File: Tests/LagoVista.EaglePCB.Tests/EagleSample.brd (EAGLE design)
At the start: 100 x 80 mm, 4 parts

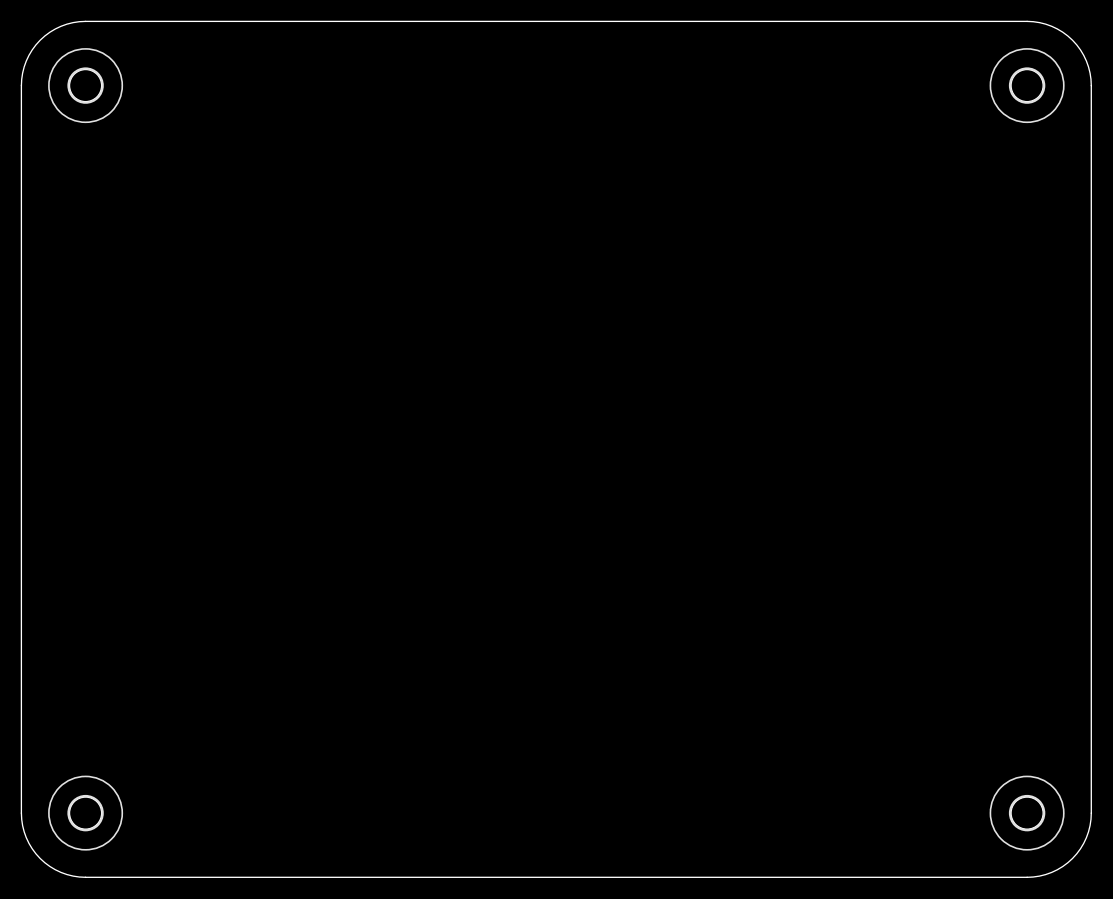
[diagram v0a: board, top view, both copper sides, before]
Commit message: rendering eagle lines
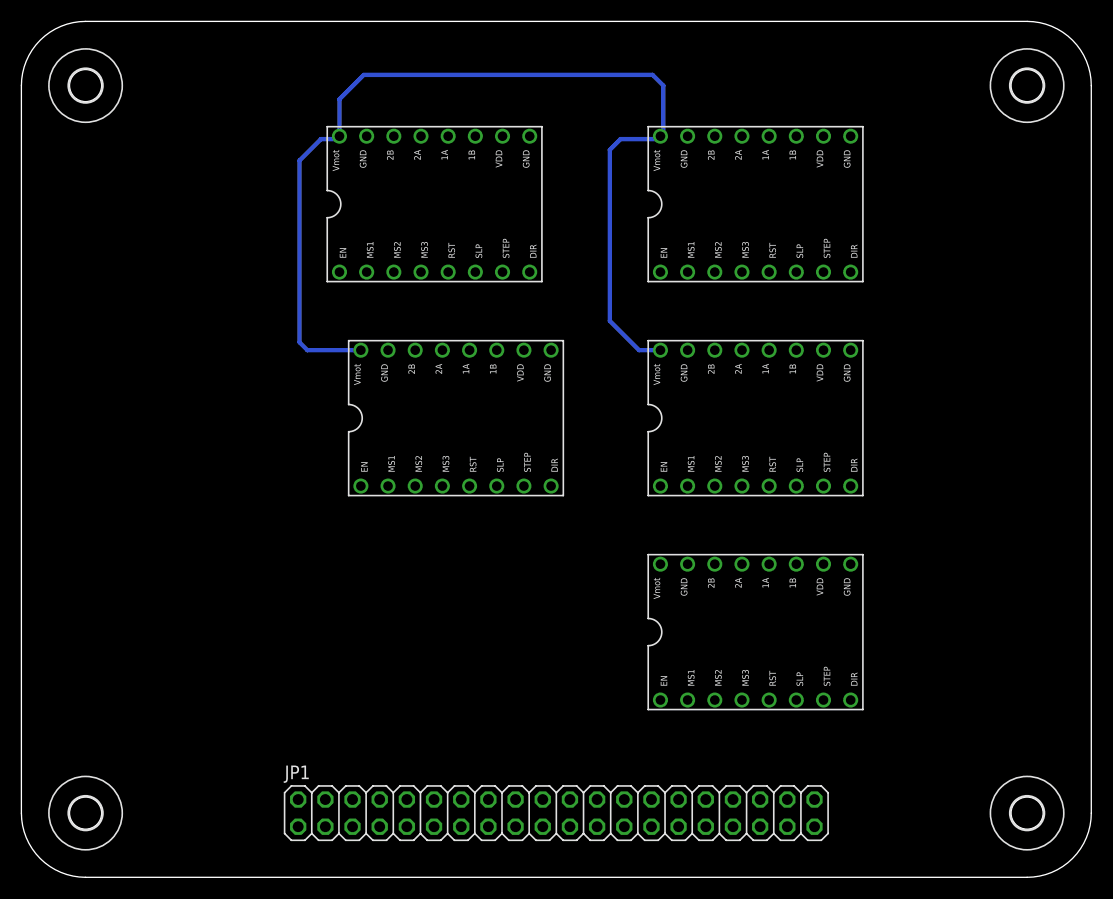
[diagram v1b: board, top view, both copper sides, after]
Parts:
- added JP1: (no value), pinhead:2X20
- added U$5, U$6, U$7, U$8, U$9: A4988BREAKOUT, RepRapjr:A4988BREAKOUT
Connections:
- new net GND: U$5.GND, U$5.GND@0, U$6.GND, U$6.GND@0, U$7.GND, U$7.GND@0, U$8.GND, U$8.GND@0, U$9.GND, U$9.GND@0
- new net VDD: U$5.VDD, U$6.VDD, U$7.VDD, U$8.VDD, U$9.VDD
- new net VMOT: U$5.VMOT, U$6.VMOT, U$7.VMOT, U$8.VMOT, U$9.VMOT
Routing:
- net VMOT: track 0.00 -> 94.7 mm
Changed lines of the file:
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@@
 <layer number="48" name="Document" color="7" fill="1" visible="yes" active="yes"/>
 <layer number="49" name="Reference" color="7" fill="1" visible="yes" active="yes"/>
+<layer number="50" name="dxf" color="7" fill="1" visible="yes" active="yes"/>
 <layer number="51" name="tDocu" color="7" fill="1" visible="yes" active="yes"/>
 <layer number="52" name="bDocu" color="7" fill="1" visible="yes" active="yes"/>
+<layer number="53" name="tGND_GNDA" color="7" fill="9" visible="no" active="no"/>
+<layer number="54" name="bGND_GNDA" color="1" fill="9" visible="no" active="no"/>
+<layer number="56" name="wert" color="7" fill="1" visible="yes" active="yes"/>
 <layer number="90" name="Modules" color="5" fill="1" visible="no" active="no"/>
 <layer number="91" name="Nets" color="2" fill="1" visible="no" active="no"/>
@@
 <layer number="97" name="Info" color="7" fill="1" visible="no" active="no"/>
 <layer number="98" name="Guide" color="6" fill="1" visible="no" active="no"/>
+<layer number="100" name="Muster" color="7" fill="1" visible="no" active="no"/>
+<layer number="101" name="Patch_Top" color="12" fill="4" visible="yes" active="yes"/>
+<layer number="102" name="Vscore" color="7" fill="1" visible="yes" active="yes"/>
+<layer number="103" name="tMap" color="7" fill="1" visible="yes" active="yes"/>
+<layer number="104" name="Name" color="7" fill="1" visible="yes" active="yes"/>
+<layer number="105" name="tPlate" color="7" fill="1" visible="yes" active="yes"/>
+<layer number="106" name="bPlate" color="7" fill="1" visible="yes" active="yes"/>
+<layer number="107" name="Crop" color="7" fill="1" visible="yes" active="yes"/>
+<layer number="116" name="Patch_BOT" color="9" fill="4" visible="yes" active="yes"/>
+<layer number="121" name="_tsilk" color="7" fill="1" visible="yes" active="yes"/>
+<layer number="122" name="_bsilk" color="7" fill="1" visible="yes" active="yes"/>
+<layer number="151" name="HeatSink" color="7" fill="1" visible="yes" active="yes"/>
+<layer number="200" name="200bmp" color="1" fill="10" visible="yes" active="yes"/>
+<layer number="201" name="201bmp" color="2" fill="10" visible="yes" active="yes"/>
+<layer number="202" name="202bmp" color="3" fill="10" visible="yes" active="yes"/>
+<layer number="203" name="203bmp" color="4" fill="10" visible="yes" active="yes"/>
+<layer number="204" name="204bmp" color="5" fill="10" visible="yes" active="yes"/>
+<layer number="205" name="205bmp" color="6" fill="10" visible="yes" active="yes"/>
+<layer number="206" name="206bmp" color="7" fill="10" visible="yes" active="yes"/>
+<layer number="207" name="207bmp" color="8" fill="10" visible="yes" active="yes"/>
+<layer number="208" name="208bmp" color="9" fill="10" visible="yes" active="yes"/>
+<layer number="250" name="Descript" color="3" fill="1" visible="no" active="no"/>
+<layer number="251" name="SMDround" color="12" fill="11" visible="no" active="no"/>
+<layer number="254" name="cooling" color="7" fill="1" visible="yes" active="yes"/>
 </layers>
 <board>
@@
 <element name="U$3" library="holes" package="3,0" value="" x="94" y="6"/>
 <element name="U$4" library="holes" package="3,0" value="" x="94" y="74"/>
+<element name="U$5" library="RepRapjr" package="A4988BREAKOUT" value="A4988BREAKOUT" x="61" y="68"/>
+<element name="U$6" library="RepRapjr" package="A4988BREAKOUT" value="A4988BREAKOUT" x="61" y="48"/>
+<element name="U$7" library="RepRapjr" package="A4988BREAKOUT" value="A4988BREAKOUT" x="61" y="28"/>
+<element name="U$8" library="RepRapjr" package="A4988BREAKOUT" value="A4988BREAKOUT" x="31" y="68"/>
+<element name="U$9" library="RepRapjr" package="A4988BREAKOUT" value="A4988BREAKOUT" x="33" y="48"/>
+<element name="JP1" library="pinhead" package="2X20" value="" x="50" y="6"/>
 </elements>
 <signals>
+<signal name="GND">
+<contactref element="U$5" pad="GND@0"/>
+<contactref element="U$5" pad="GND"/>
+<contactref element="U$6" pad="GND@0"/>
+<contactref element="U$6" pad="GND"/>
+<contactref element="U$7" pad="GND@0"/>
+<contactref element="U$7" pad="GND"/>
+<contactref element="U$8" pad="GND@0"/>
+<contactref element="U$8" pad="GND"/>
+<contactref element="U$9" pad="GND@0"/>
+<contactref element="U$9" pad="GND"/>
+<wire x1="62.27" y1="69.27" x2="77.51" y2="69.27" width="0" layer="19" extent="1-1"/>
+<wire x1="47.51" y1="69.27" x2="62.27" y2="69.27" width="0" layer="19" extent="1-1"/>
+<wire x1="32.27" y1="69.27" x2="47.51" y2="69.27" width="0" layer="19" extent="1-1"/>
+<wire x1="77.51" y1="49.27" x2="77.51" y2="69.27" width="0" layer="19" extent="1-1"/>
+<wire x1="77.51" y1="29.27" x2="77.51" y2="49.27" width="0" layer="19" extent="1-1"/>
+<wire x1="62.27" y1="29.27" x2="77.51" y2="29.27" width="0" layer="19" extent="1-1"/>
+<wire x1="49.51" y1="49.27" x2="62.27" y2="29.27" width="0" layer="19" extent="1-1"/>
+<wire x1="34.27" y1="49.27" x2="49.51" y2="49.27" width="0" layer="19" extent="1-1"/>
+<wire x1="62.27" y1="49.27" x2="77.51" y2="49.27" width="0" layer="19" extent="1-1"/>
+</signal>
+<signal name="VDD">
+<contactref element="U$5" pad="VDD"/>
+<contactref element="U$6" pad="VDD"/>
+<contactref element="U$7" pad="VDD"/>
+<contactref element="U$8" pad="VDD"/>
+<contactref element="U$9" pad="VDD"/>
+<wire x1="74.97" y1="49.27" x2="74.97" y2="69.27" width="0" layer="19" extent="1-1"/>
+<wire x1="74.97" y1="29.27" x2="74.97" y2="49.27" width="0" layer="19" extent="1-1"/>
+<wire x1="44.97" y1="69.27" x2="74.97" y2="69.27" width="0" layer="19" extent="1-1"/>
+<wire x1="46.97" y1="49.27" x2="74.97" y2="29.27" width="0" layer="19" extent="1-1"/>
+</signal>
+<signal name="VMOT">
+<contactref element="U$5" pad="VMOT"/>
+<contactref element="U$6" pad="VMOT"/>
+<contactref element="U$7" pad="VMOT"/>
+<contactref element="U$8" pad="VMOT"/>
+<contactref element="U$9" pad="VMOT"/>
+<wire x1="29.73" y1="69.27" x2="29.73" y2="72.73" width="0.4064" layer="16"/>
+<wire x1="29.73" y1="72.73" x2="32" y2="75" width="0.4064" layer="16"/>
+<wire x1="32" y1="75" x2="59" y2="75" width="0.4064" layer="16"/>
+<wire x1="59" y1="75" x2="60" y2="74" width="0.4064" layer="16"/>
+<wire x1="60" y1="74" x2="60" y2="69.54" width="0.4064" layer="16"/>
+<wire x1="60" y1="69.54" x2="59.73" y2="69.27" width="0.4064" layer="16"/>
+<wire x1="59.73" y1="49.27" x2="57.73" y2="49.27" width="0.4064" layer="16"/>
+<wire x1="57.73" y1="49.27" x2="55" y2="52" width="0.4064" layer="16"/>
+<wire x1="55" y1="52" x2="55" y2="68" width="0.4064" layer="16"/>
+<wire x1="55" y1="68" x2="56" y2="69" width="0.4064" layer="16"/>
+<wire x1="56" y1="69" x2="59.46" y2="69" width="0.4064" layer="16"/>
+<wire x1="59.46" y1="69" x2="59.73" y2="69.27" width="0.4064" layer="16"/>
+<wire x1="59.73" y1="29.27" x2="59.73" y2="49.27" width="0" layer="19" extent="1-1"/>
+<wire x1="31.73" y1="49.27" x2="26.73" y2="49.27" width="0.4064" layer="16"/>
+<wire x1="26.73" y1="49.27" x2="26" y2="50" width="0.4064" layer="16"/>
+<wire x1="26" y1="50" x2="26" y2="67" width="0.4064" layer="16"/>
+<wire x1="26" y1="67" x2="28" y2="69" width="0.4064" layer="16"/>
+<wire x1="28" y1="69" x2="29.46" y2="69" width="0.4064" layer="16"/>
+<wire x1="29.46" y1="69" x2="29.73" y2="69.27" width="0.4064" layer="16"/>
+</signal>
 </signals>
 </board>
